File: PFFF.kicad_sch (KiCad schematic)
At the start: 14 parts, among them J1 Conn_01x02, J2 Conn_01x02, J3 Conn_01x03, J4 Conn_01x03, U1 TPS61099YFFT

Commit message: fake change
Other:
- note added: "debug"
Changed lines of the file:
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@@
+		)
+	)
+	(text "debug"
+		(exclude_from_sim no)
+		(at 233.68 35.814 0)
+		(effects
+			(font
+				(size 1.27 1.27)
+			)
 		)
 	)

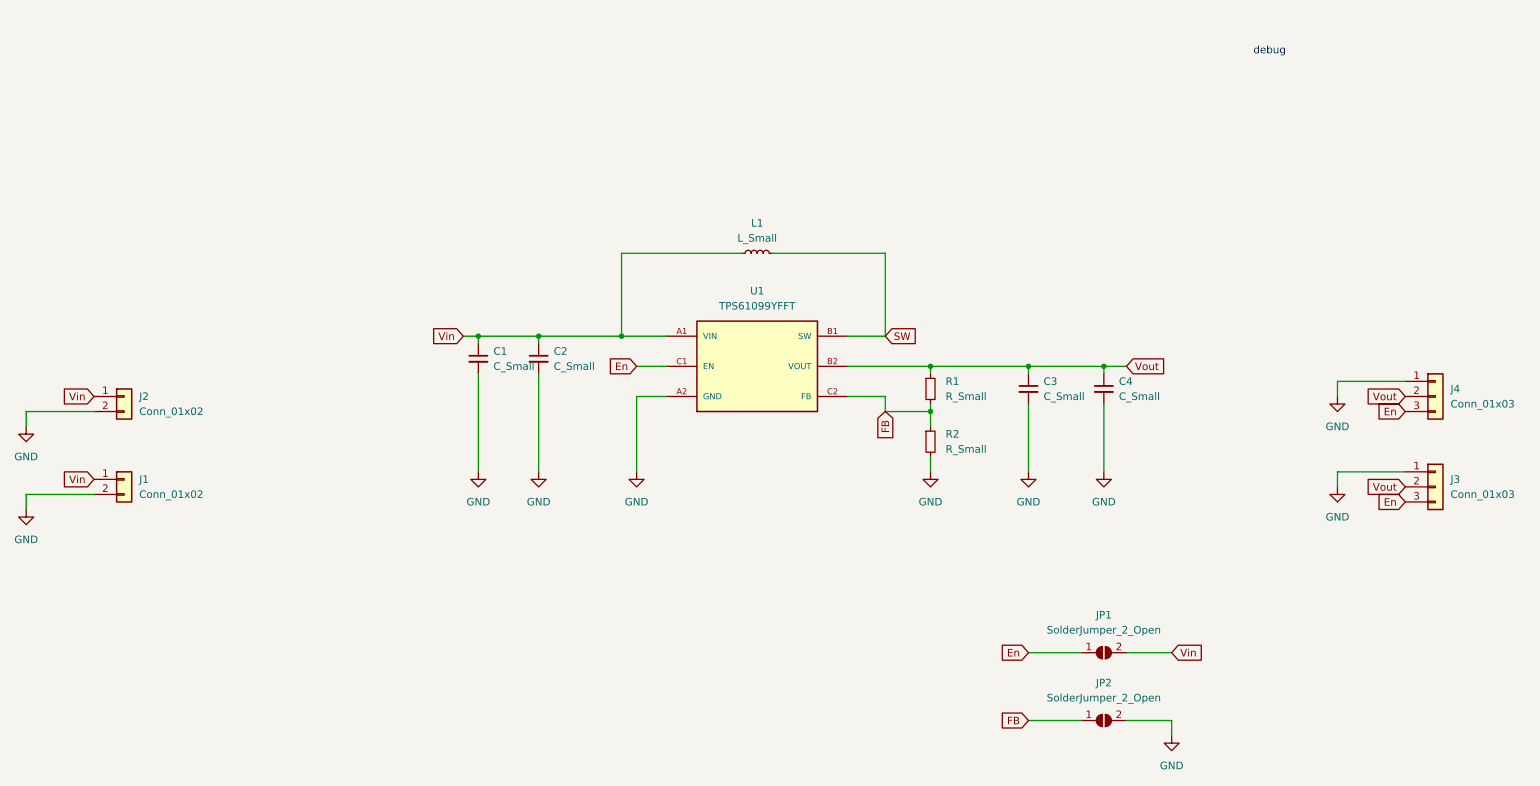
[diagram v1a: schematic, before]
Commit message: add all USB Type-C
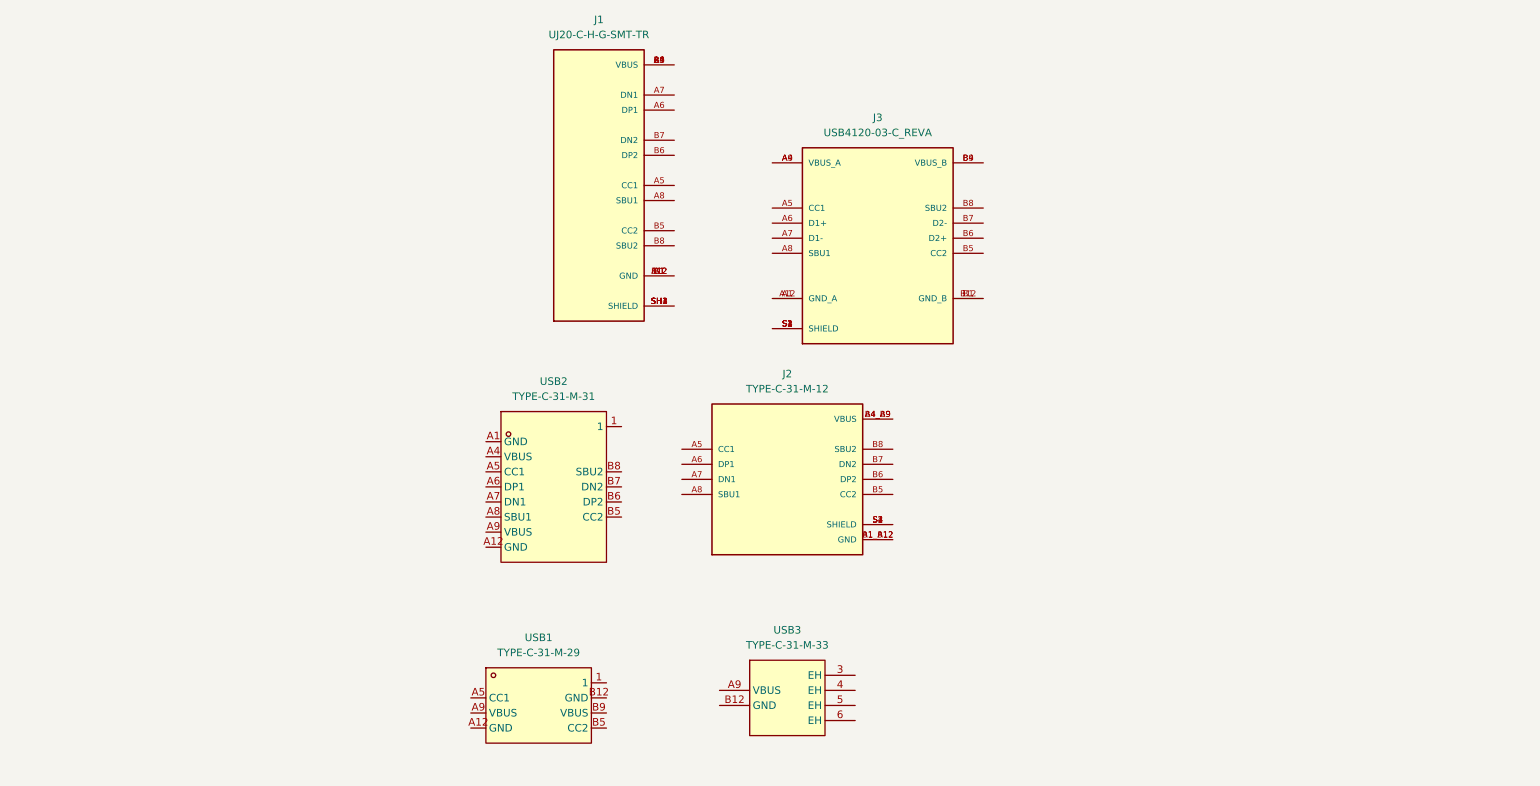
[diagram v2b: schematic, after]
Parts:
- removed C1, C2, C3, C4: C_Small, Capacitor_SMD:C_0805_2012Metric, symbol Device:C_Small
- removed J1, J2: Conn_01x02, Connector_PinHeader_2.54mm:PinHeader_1x02_P2.54mm_Vertical, symbol Connector_Generic:Conn_01x02
- removed J3, J4: Conn_01x03, Connector_PinHeader_2.54mm:PinHeader_1x03_P2.54mm_Vertical, symbol Connector_Generic:Conn_01x03
- removed JP1, JP2: SolderJumper_2_Open, Jumper:SolderJumper-2_P1.3mm_Open_RoundedPad1.0x1.5mm, symbol Jumper:SolderJumper_2_Open
- removed L1: L_Small, Inductor_SMD:L_1008_2520Metric, symbol Device:L_Small
- removed R1, R2: R_Small, Resistor_SMD:R_0805_2012Metric, symbol Device:R_Small
- removed U1: TPS61099YFFT, Converter_DCDC_custom:BGA6N40P3X2_122X88X62N, symbol Converter_DCDC_custom:TPS61099YFFT
- added J1: UJ20-C-H-G-SMT-TR, Snapeda:UJ20-C-H-G-SMT-TR_CUI_UJ20-C-H-G-SMT-TR, symbol Snapeda_kicad_sym:UJ20-C-H-G-SMT-TR
- added J2: TYPE-C-31-M-12, Snapeda:TYPE-C-31-M-12_HRO_TYPE-C-31-M-12, symbol Snapeda_kicad_sym:TYPE-C-31-M-12
- added J3: USB4120-03-C_REVA, Snapeda:USB4120-03-C_REVA_GCT_USB4120-03-C_REVA, symbol Snapeda_kicad_sym:USB4120-03-C_REVA
- added USB1: TYPE-C-31-M-29, Snapeda:easyeda2kicad_USB-C-SMD_TYPE-C-31-M-29, symbol Snapeda_kicad_sym:TYPE-C-31-M-29
- added USB2: TYPE-C-31-M-31, Snapeda:easyeda2kicad_USB-C-SMD_TYPE-C-31-M-31, symbol Snapeda_kicad_sym:TYPE-C-31-M-31
- added USB3: TYPE-C-31-M-33, Snapeda:easyeda2kicad_USB-C-TH_TYPE-C-31-M-33, symbol Snapeda_kicad_sym:TYPE-C-31-M-33
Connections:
- new net: J1.A1 (GND), J1.A12 (GND), J1.B1 (GND), J1.B12 (GND)
- new net: J1.A4 (VBUS), J1.A9 (VBUS), J1.B4 (VBUS), J1.B9 (VBUS)
- new net: J1.SH1 (SHIELD), J1.SH2 (SHIELD), J1.SH3 (SHIELD), J1.SH4 (SHIELD)
- new net: J3.A1 (GND_A), J3.A12 (GND_A)
- new net: J3.A4 (VBUS_A), J3.A9 (VBUS_A)
- new net: J3.B1 (GND_B), J3.B12 (GND_B)
- new net: J3.B4 (VBUS_B), J3.B9 (VBUS_B)
- new net: J3.S1 (SHIELD), J3.S2 (SHIELD), J3.S3 (SHIELD), J3.S4 (SHIELD)
- new net: J2.A1_B12 (GND), J2.B1_A12 (GND)
- new net: J2.A4_B9 (VBUS), J2.B4_A9 (VBUS)
- new net: J2.S1 (SHIELD), J2.S2 (SHIELD), J2.S3 (SHIELD), J2.S4 (SHIELD)
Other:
- note removed: "debug"
